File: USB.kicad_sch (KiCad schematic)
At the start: 109 parts, among them J1 USB_A, J3 USB_A, J4 USB_A, J5 USB_A, J6 Conn_01x04, J7 USB_C_Receptacle_USB2.0_16P, U3 GL3523-OTY30, U4 USB-PD, U5 LPW5209AB5F, U6 LPW5209AB5F, U7 LPW5209AB5F, U8 LPW5209AB5F, U9 MX25L1006EMI-10G, Y1 Crystal 25MHz 2016

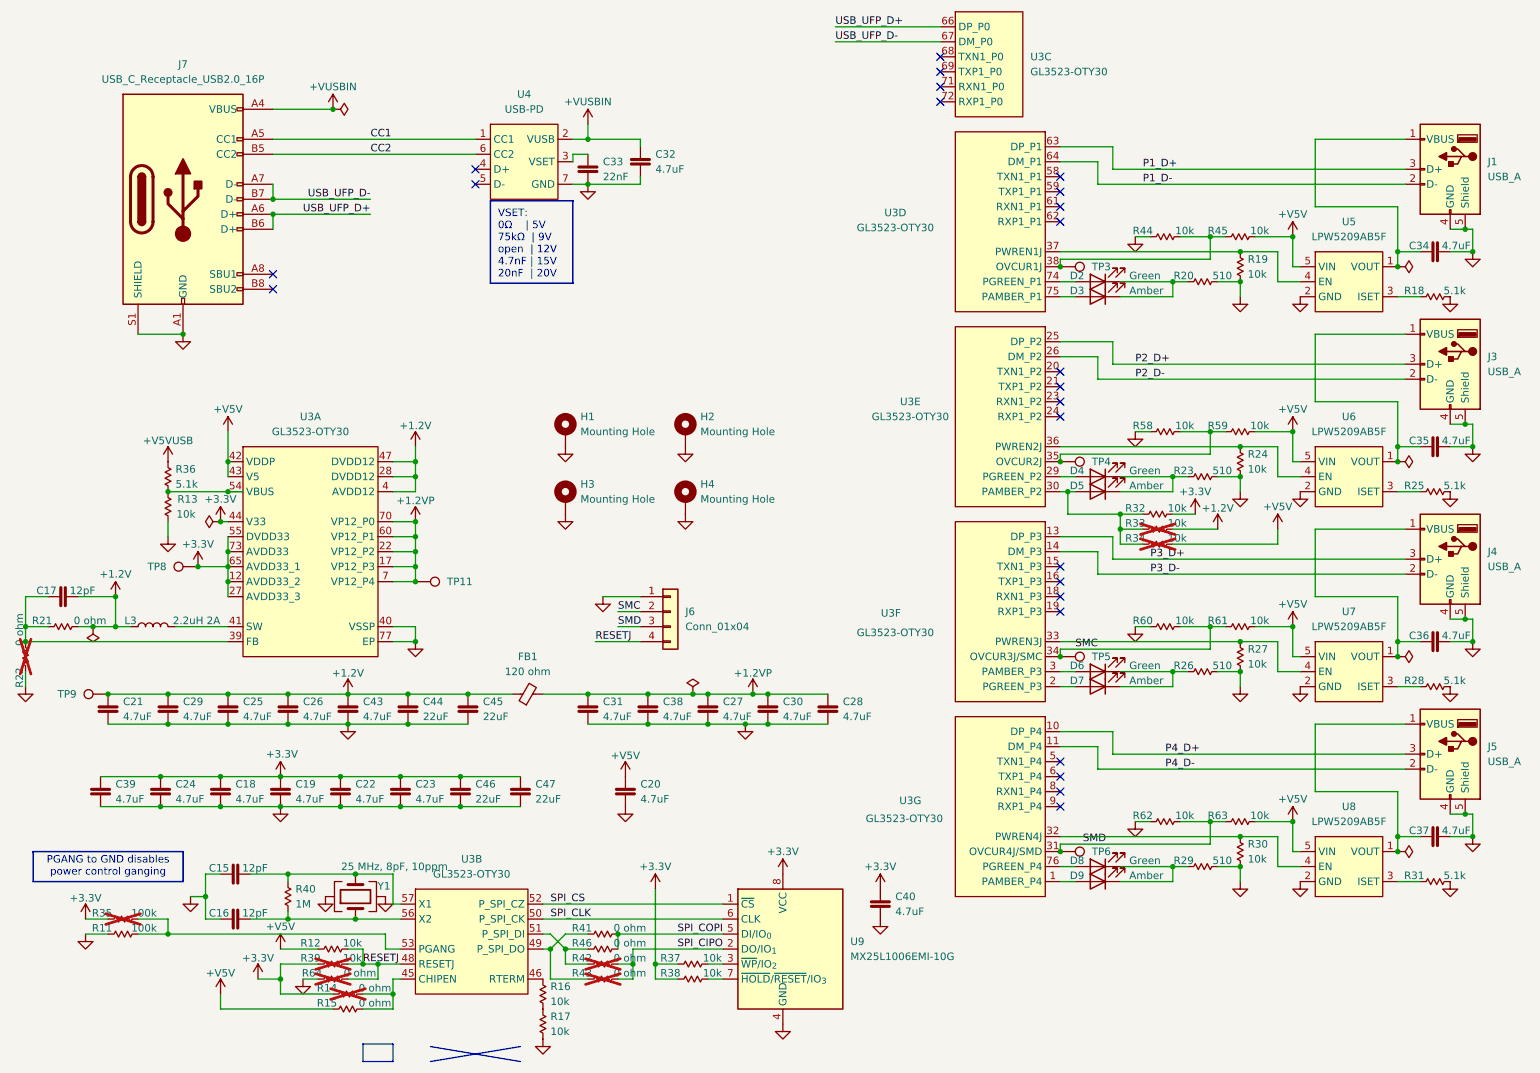
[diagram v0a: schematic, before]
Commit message: add second power circuit
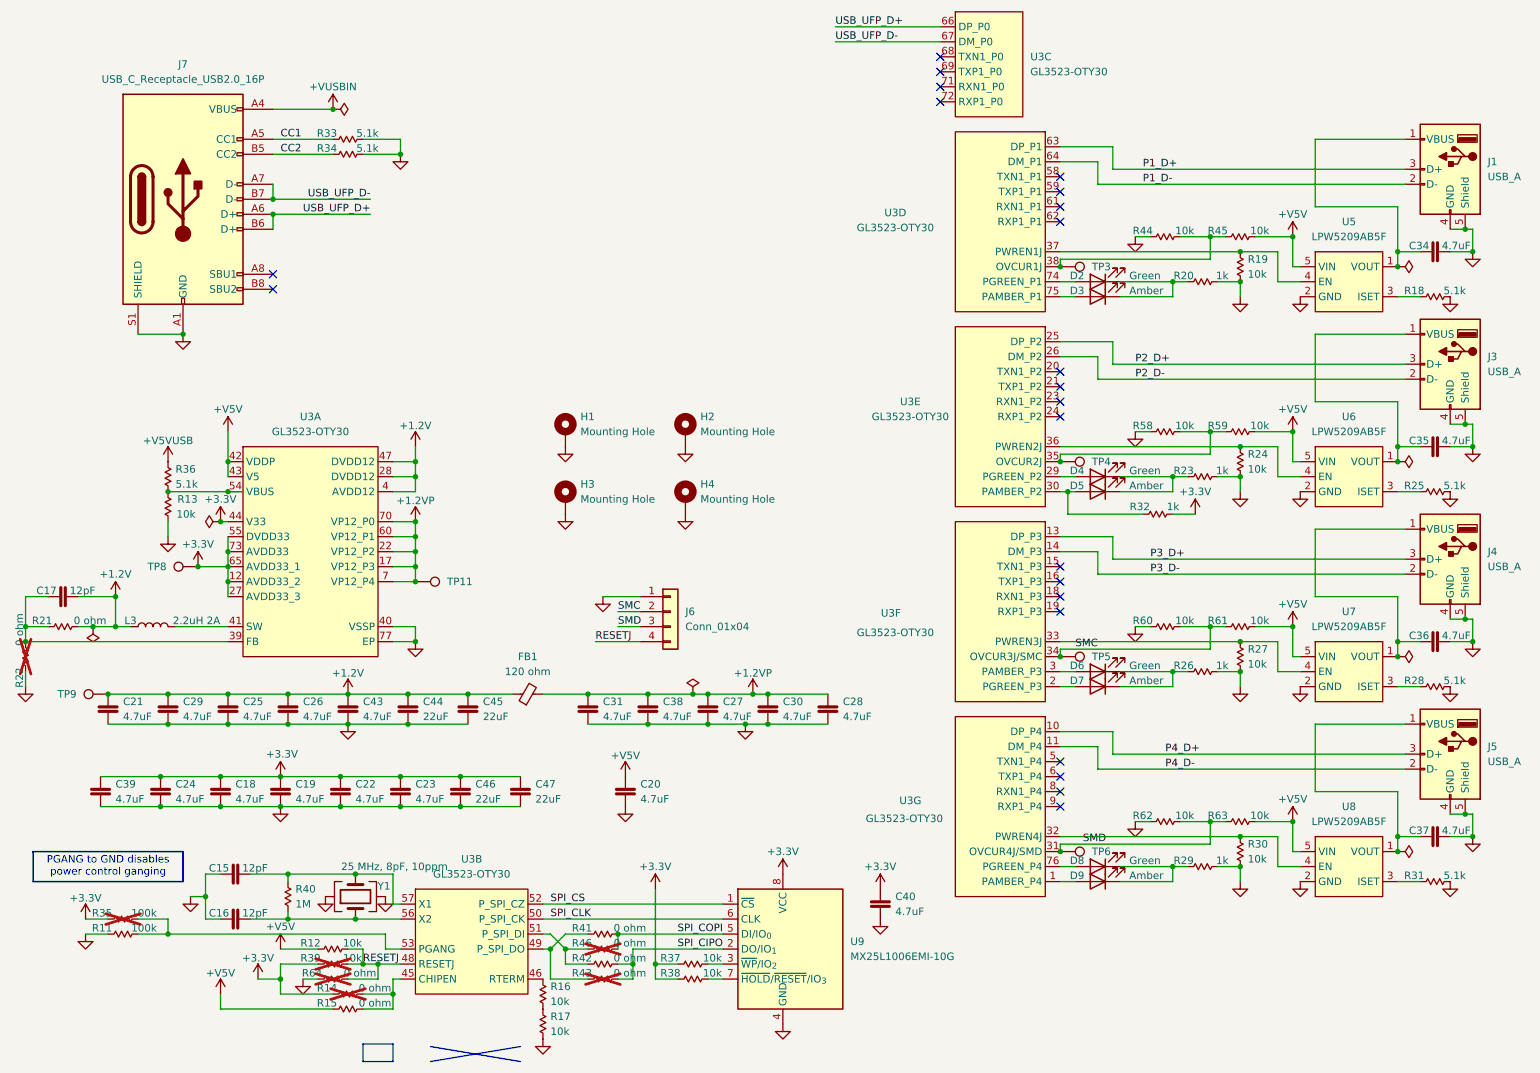
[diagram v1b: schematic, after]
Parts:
- removed C32: Cap 4.7uF 0402, Capacitor_SMD:C_0402_1005Metric, symbol Kalid:Cap 4.7uF 0402
- removed C33: Cap 22nF 0402, Capacitor_SMD:C_0402_1005Metric, symbol Kalid:Cap 22nF 0402
- removed R32, R33, R34: R 10k 0402, Resistor_SMD:R_0402_1005Metric, symbol Kalid:R 10k 0402
- removed U4: USB-PD, Package_DFN_QFN:DFN-6-1EP_2x2mm_P0.65mm_EP1x1.6mm, symbol Kalid:HUSB237-AA001-DN06R
- added R32: R 1k 0402, Resistor_SMD:R_0402_1005Metric, symbol Kalid:R 1k 0402
- added R33, R34: R 5.1k 0402, Resistor_SMD:R_0402_1005Metric, symbol Kalid:R 5.1k 0402
- R20, R23, R26, R29: symbol Kalid:R 510 0402 -> Kalid:R 1k 0402; LCSC C25123 -> C11702; MPN 0402WGF5100TCE -> 0402WGF1001TCE; Manufacturer UNI-ROYAL(Uniroyal Elec) -> uni-royal(uniroyal elec); Val 510 -> 1k
- R42: now fitted; now in the parts list
- R46: now not fitted; now left out of the parts list
- U9: footprint Package_SO:SOIC-8_5.3x5.3mm_P1.27mm -> Package_SO:SOP-8_3.76x4.96mm_P1.27mm
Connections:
- net +3.3V: now also R32.1
- net CC1: now also R33.2
- net CC2: now also R34.2
- net GND: now also R33.1, R34.1
- net at D5.2 (A), U3.30 (PAMBER_P2): now also R32.2
- no-connect marks 24 -> 22
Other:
- note removed: "VSET: 0Ω | 5V 75kΩ | 9V open | 12V 4.7nF | 15V 20nF | 20V"

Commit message: evt5: Release
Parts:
- R20, R23, R26, R29: value R 510 0402 -> R 1k 0402
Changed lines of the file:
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@@
 	(title_block
 		(title "Kalid")
-		(date "2025-09-18")
+		(date "2025-11-09")
 		(rev "EVT5")
 	)
@@
 			)
 		)
-		(property "Value" "R 510 0402"
+		(property "Value" "R 1k 0402"
 			(at 218.44 149.86 90)
 			(effects
@@
 			)
 		)
-		(property "Value" "R 510 0402"
+		(property "Value" "R 1k 0402"
 			(at 218.44 50.8 90)
 			(effects
@@
 			)
 		)
-		(property "Value" "R 510 0402"
+		(property "Value" "R 1k 0402"
 			(at 218.44 83.82 90)
 			(effects
@@
 			)
 		)
-		(property "Value" "R 510 0402"
+		(property "Value" "R 1k 0402"
 			(at 218.44 116.84 90)
 			(effects
